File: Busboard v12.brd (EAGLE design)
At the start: 248.5 x 54 mm, 121 parts, among them J1_+15 PIN2F061.100, J2_+15 PIN2F061.100, J3_GND PIN2F061.100, J4_GND PIN2F061.100, J5_-15 PIN2F061.100, J6_-15 PIN2F061.100

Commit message: v12
- Aligned mounting holes
- All LEDS same orientation
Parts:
- moved C35 3.42 mm to (27.5, 7.51)
- moved U$1 2.06 mm to (16.8, 44.5)
- moved U$2 1.97 mm to (16.3, 7.51)
- moved C37 1.70 mm to (27.4, 19.3)
- moved C36 0.63 mm to (27.5, 44.5)
- moved LED2 0.50 mm to (44.3, 46.3)
- moved LED18 0.41 mm to (216.2, 46.3), turned to 90 degrees
- moved LED17 0.38 mm to (208.6, 46.3)
- moved LED15 0.37 mm to (182.5, 46.3), turned to 90 degrees
- moved LED16 0.33 mm to (201.0, 46.3)
- moved 8 0.26 mm to (151.2, 35.6)
- moved C34 0.22 mm to (27.4, 32.8)
- moved R1 0.22 mm to (41.0, 47.6)
- moved R16 0.21 mm to (204.8, 47.5)
- moved R10 0.20 mm to (138.3, 47.5)
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- renumbered +15V_DC_IN to +15V, -15V_DC_IN to -15V, GND_IN to GND
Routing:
- net N$15: track 0.00 -> 31.4 mm
- net GND: track 384.6 -> 369.2 mm
- net -15V: track 22.3 -> 15.0 mm
- net N$5: track 84.1 -> 81.8 mm, vias 3 -> 1
- net +15V: track 14.9 -> 16.8 mm
- net N$63: track 3.75 -> 5.11 mm
- net N$20: track 60.3 -> 59.1 mm
- net N$25: track 3.81 -> 4.68 mm
- net N$17: track 3.81 -> 4.56 mm
- net N$70: track 3.42 -> 4.13 mm
- net N$54: track 3.94 -> 4.57 mm
- net N$30: track 3.81 -> 4.43 mm
- net N$62: track 4.48 -> 3.87 mm
- net N$14: track 3.81 -> 4.31 mm
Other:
- board text added: "+15V DC IN"
- board text added: "-15V DC IN"

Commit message: Added OSLR + OSHWA marks
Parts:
- moved 4 12.0 mm to (130.1, 25.1)
- moved 5 12.0 mm to (130.1, 36.6)
- moved 6 12.0 mm to (130.1, 13.7)
- moved C15 12.0 mm to (74.2, 40.0)
- moved +15V 12.0 mm to (8.43, 37.8)
- moved -15V 12.0 mm to (8.43, 12.4)
- moved 1 12.0 mm to (97.1, 25.1)
- moved 10 12.0 mm to (196.2, 25.1)
- moved 11 12.0 mm to (196.0, 36.6)
- moved 12 12.0 mm to (196.0, 13.7)
- moved 13 12.0 mm to (229.2, 25.1)
- moved 14 12.0 mm to (229.2, 36.6)
- moved 15 12.0 mm to (228.9, 13.7)
- moved 2 12.0 mm to (97.1, 36.6)
- moved 3 12.0 mm to (97.1, 13.7)
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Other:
- board text added: "/Users/Bruno/Desktop/OSLR/PCB_Assets/22_bPlace.bmp"

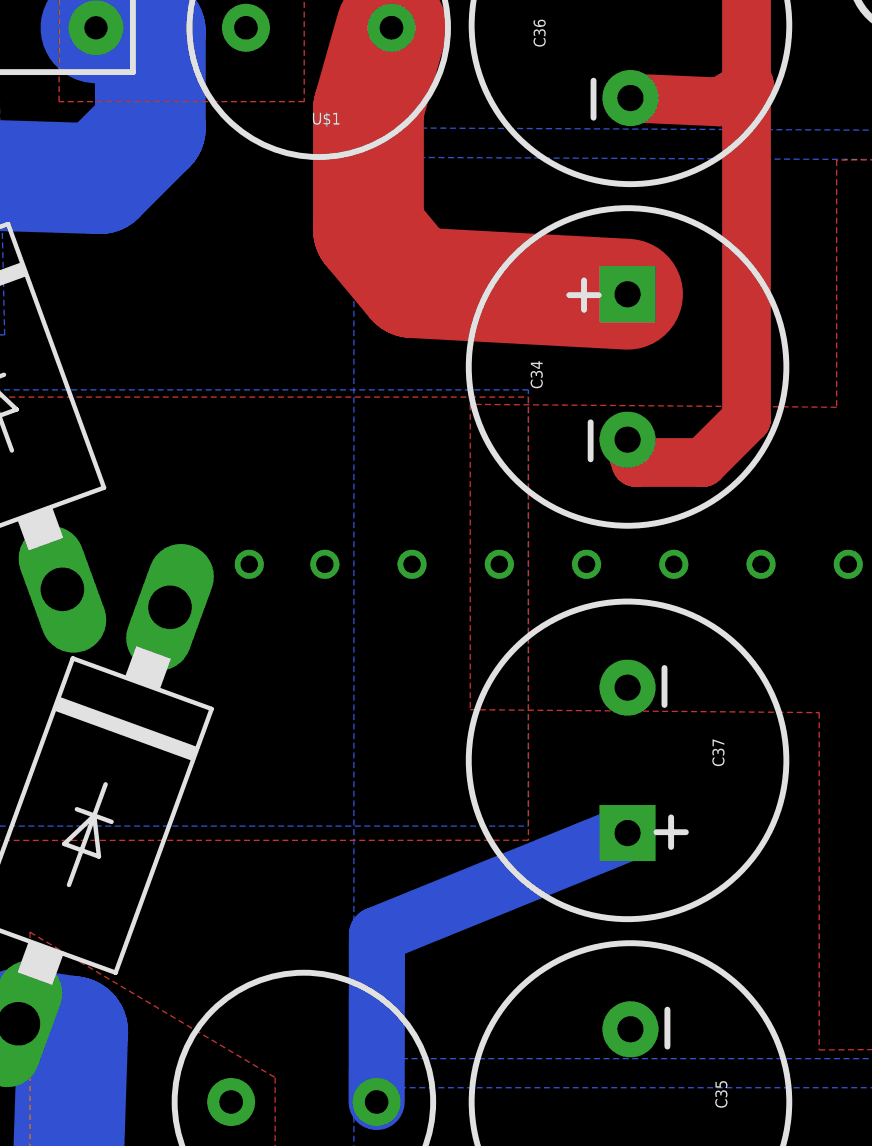
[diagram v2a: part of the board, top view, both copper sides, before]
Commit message: updated .sch and .brd
i did another check over everything to make sure it lined up with the power sandwich, and added a 0.1uf 50v cap just after the inductor/ferrite bead to hopefully reduce ripple at the input.
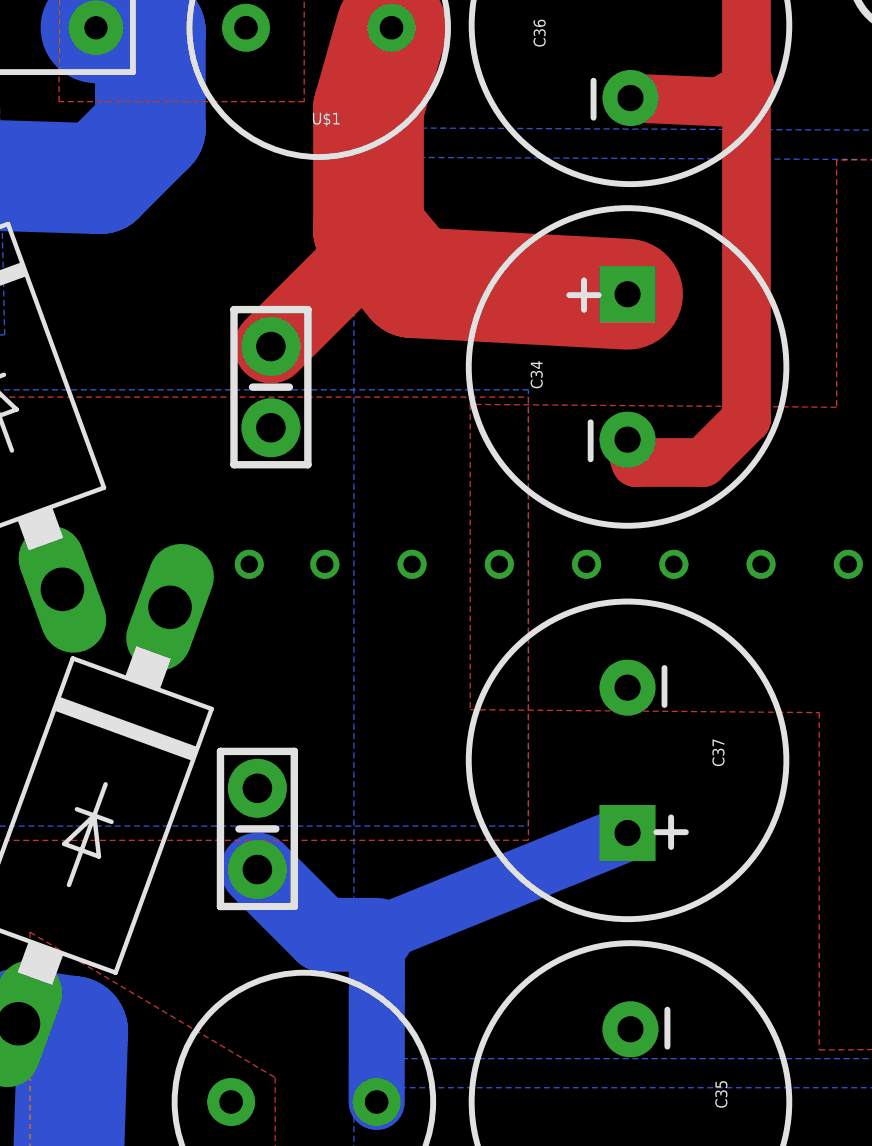
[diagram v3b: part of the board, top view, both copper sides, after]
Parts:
- added C10, C11: 0.1uf, SparkFun-Capacitors:CAP-PTH-SMALL-KIT
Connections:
- net +15V: now also C11.1
- net -15V: now also C10.2
- net GND: now also C10.1, C11.2
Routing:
- net +15V: track 16.8 -> 22.2 mm
- net -15V: track 15.0 -> 20.1 mm
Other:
- board text added: "7805"
- board text added: "7812"
- board text added: "7912"
- board text added: "C16"
- board text added: "C17"
- board text added: "C22"
- board text added: "C23"
- board text added: "C27"
- board text added: "C28"
- board text added: "C32"
- board text added: "C33"
- board text added: "C34"
- board text added: "C35"
- board text added: "C36"
- board text added: "C37"
- board text added: "C4"
- board text added: "C5"
- board text added: "C8"
- board text added: "C9"
- board text added: "F1"
- board text added: "F2"
- board text added: "GND"
- board text added: "U$1"
- board text added: "U$2"

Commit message: Add files via upload
Fixing some dumb mistakes based on building the v12 prototype. had some backward caps and should have picked a lower trip thresh for the polyfuse.
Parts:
- turned C17 to 0 degrees
- turned C23 to 0 degrees
- turned C28 to 0 degrees
- turned C33 to 0 degrees
- turned C35 to 90 degrees
- turned C37 to 90 degrees
- turned C5 to 0 degrees
- turned C9 to 0 degrees
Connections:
- net -15V: now also C35.-, C37.-; no longer C35.+, C37.+
- net GND: now also C17.1, C23.1, C28.1, C33.1, C35.+, C37.+, C5.1, C9.1; no longer 7.GND, 9.GND, C17.2, C23.2, C28.2, C33.2, C35.-, C37.-, C5.2, C9.2
- net N$1: now also C5.2; no longer C5.1
- net N$48: now also C23.2; no longer C23.1
- net N$57: now also C28.2; no longer C28.1
- net N$64: now also C33.2; no longer C33.1
- net N$7: now also C17.2; no longer C17.1
- net N$8: now also C9.2; no longer C9.1
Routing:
- net -15V: track 20.1 -> 20.9 mm
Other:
- board text added: "-12"
